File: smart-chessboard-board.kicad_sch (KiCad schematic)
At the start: 13 parts, among them J101 Conn_01x12_MountingPin, SW101 SW_SPDT, SW102 SW_SPDT, U101 LTR-F216A, U102 74AHCT1G125

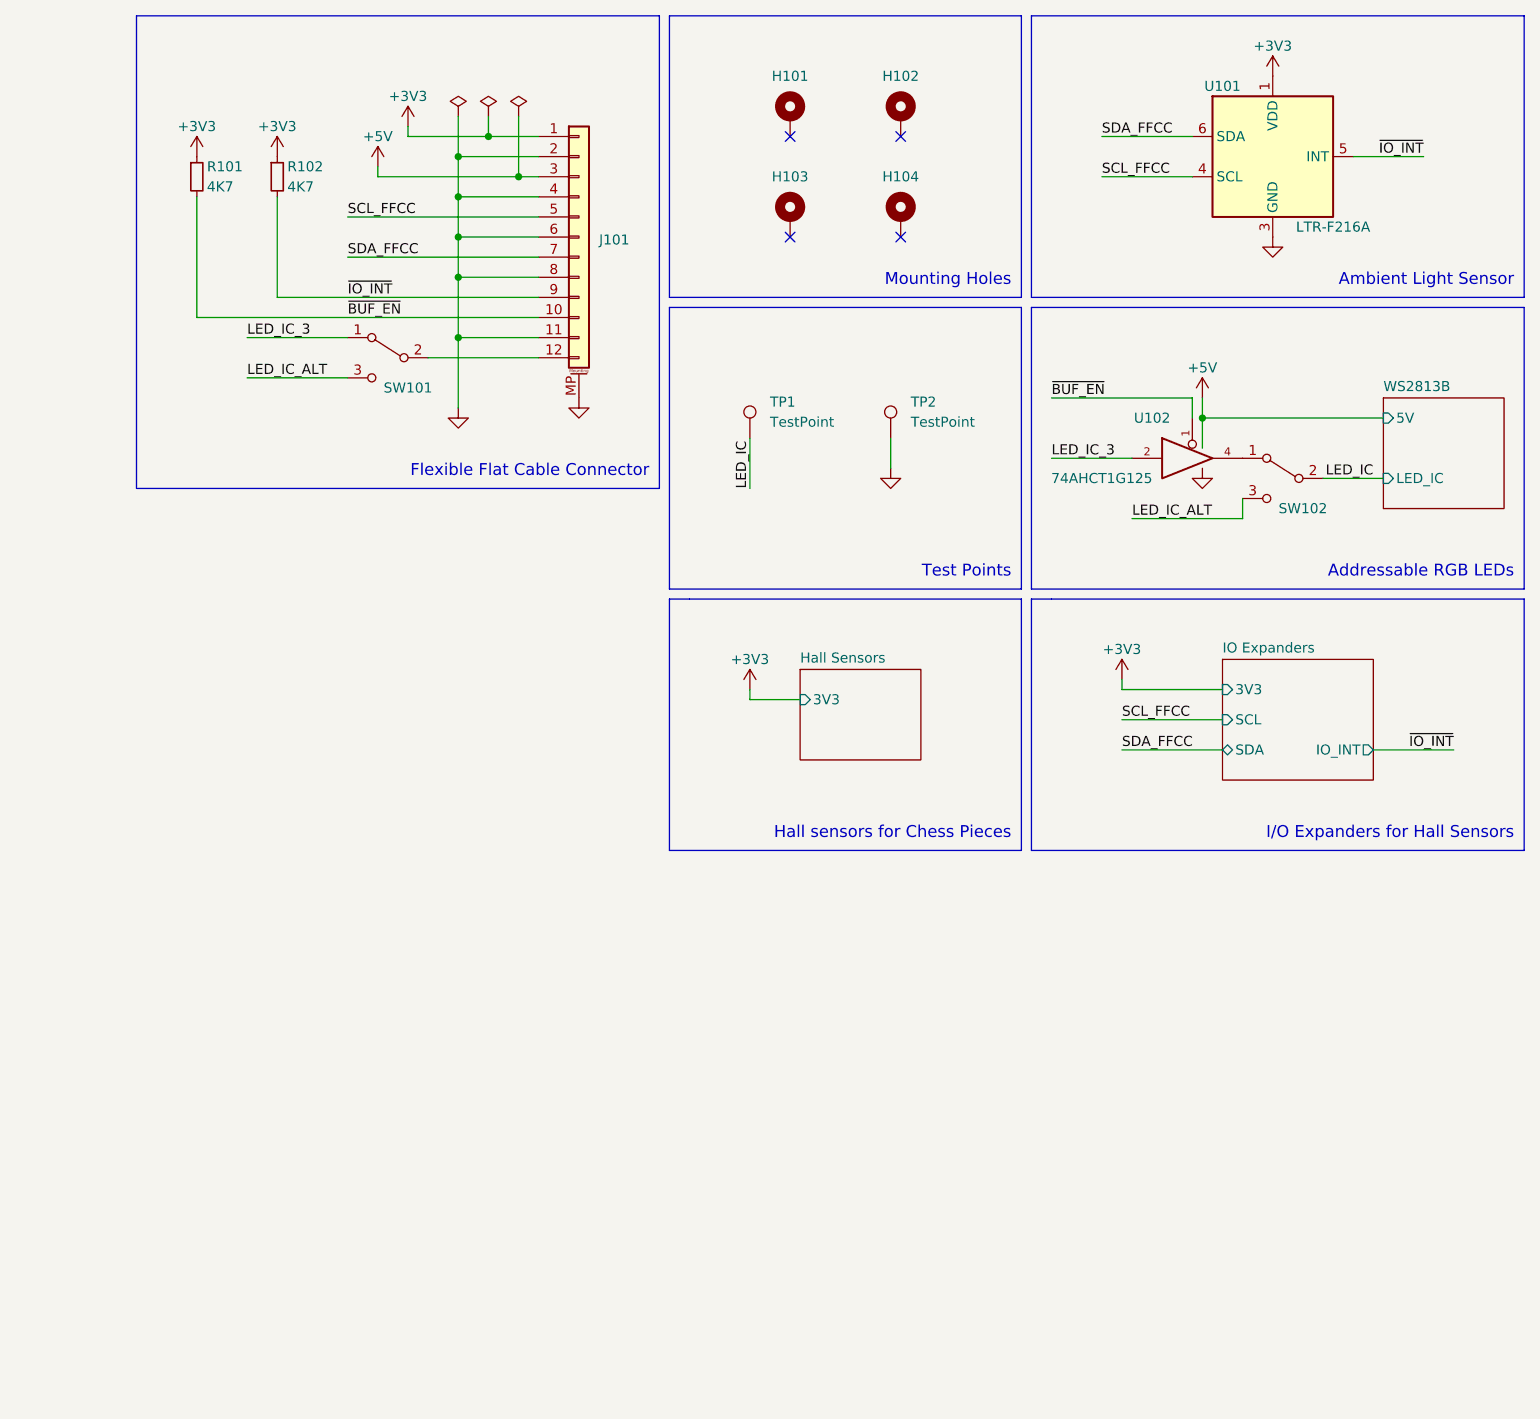
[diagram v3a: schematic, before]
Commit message: remove test points / pull-up resistors
- move pull-up resistors to controller side
- remove test points, not needed anymore
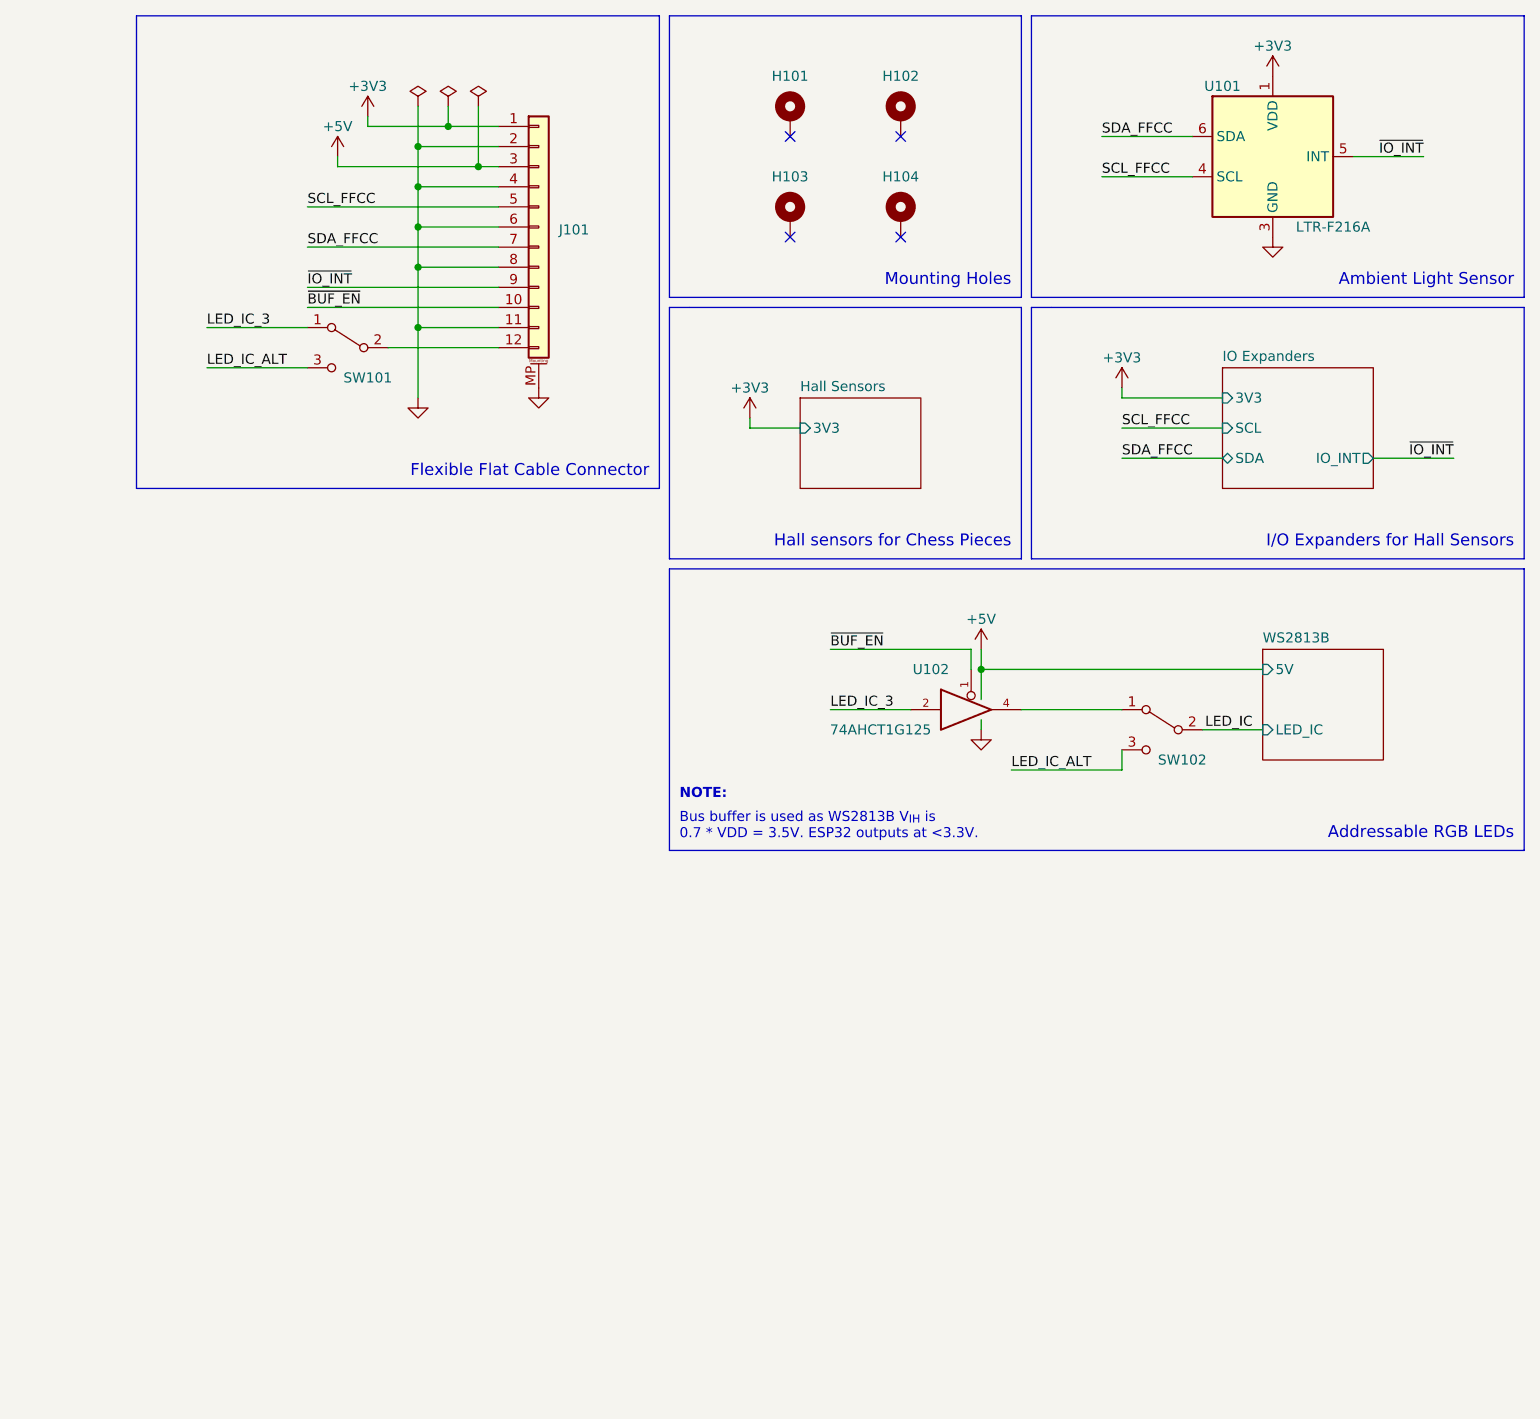
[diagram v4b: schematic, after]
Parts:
- removed R101, R102: 4K7, Resistor_SMD:R_0603_1608Metric, symbol Device:R_Small
- removed TP1, TP2: TestPoint, TestPoint:TestPoint_Pad_D2.0mm, symbol Connector:TestPoint
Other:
- note added: "Bus buffer is used as WS2813B V_{IH} is 0.7 * VDD = 3.5V. ESP32 outputs at <3.3V."
- note added: "NOTE:"
- note removed: "Test Points"
- moved on the sheet: J101, SW101, SW102, U102

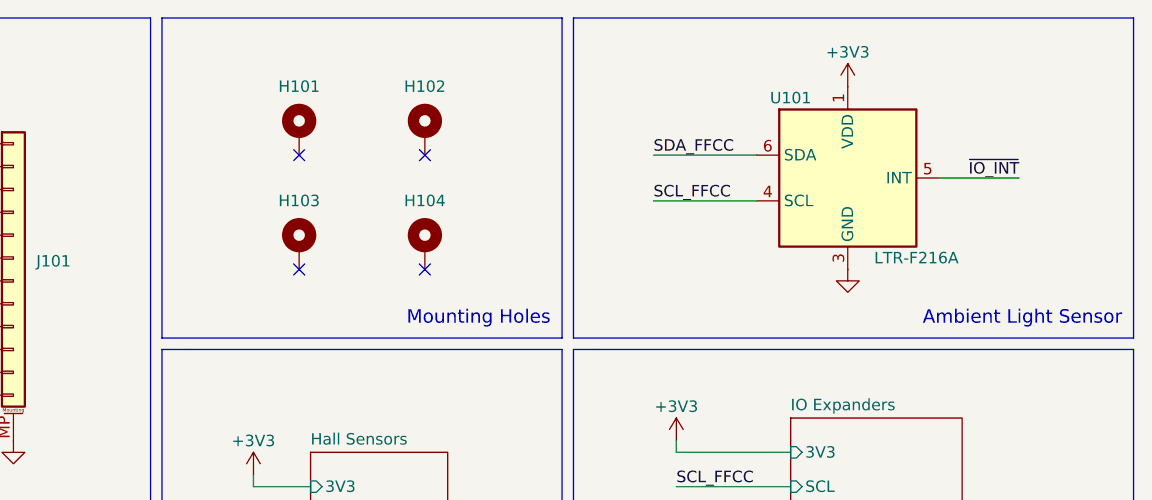
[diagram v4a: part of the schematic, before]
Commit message: add bypass caps
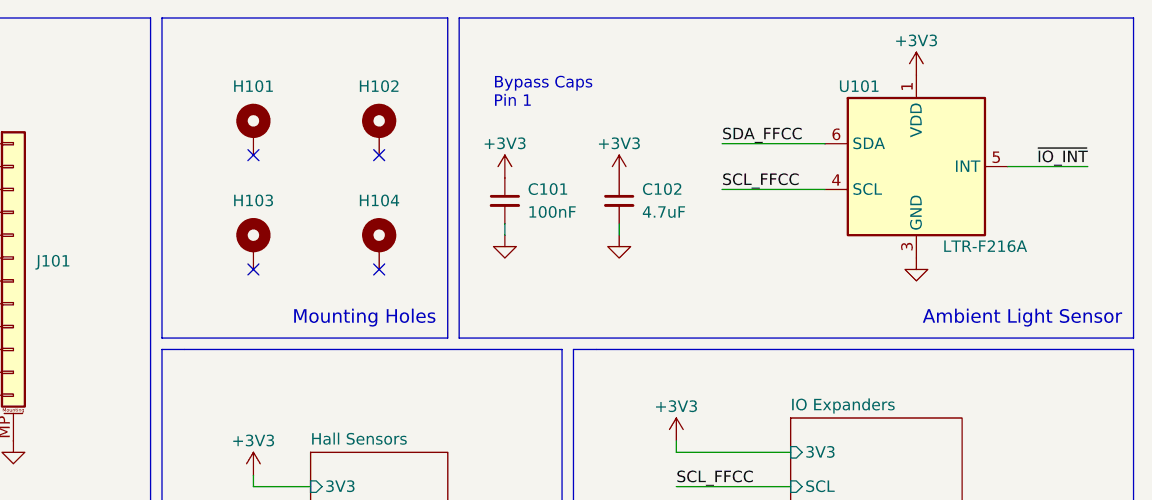
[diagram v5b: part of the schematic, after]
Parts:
- added C101: 100nF, Capacitor_SMD:C_0603_1608Metric, symbol Device:C_Small
- added C102: 4.7uF, Capacitor_SMD:C_0603_1608Metric, symbol Device:C_Small
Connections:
- net +3V3: now also C101.1, C102.1
- net GND: now also C101.2, C102.2
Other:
- note added: "Bypass Caps Pin 1"
- moved on the sheet: H101, H102, H103, H104, U101

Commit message: update datasheet and parts
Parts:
- added R101: 220, symbol Device:R_Small
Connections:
- net LED_IC: now also R101.2; no longer SW102.2 (B)
- new net: R101.1, SW102.2 (B)
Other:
- moved on the sheet: SW102, U102
